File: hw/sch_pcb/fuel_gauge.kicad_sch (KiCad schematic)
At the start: 39 parts

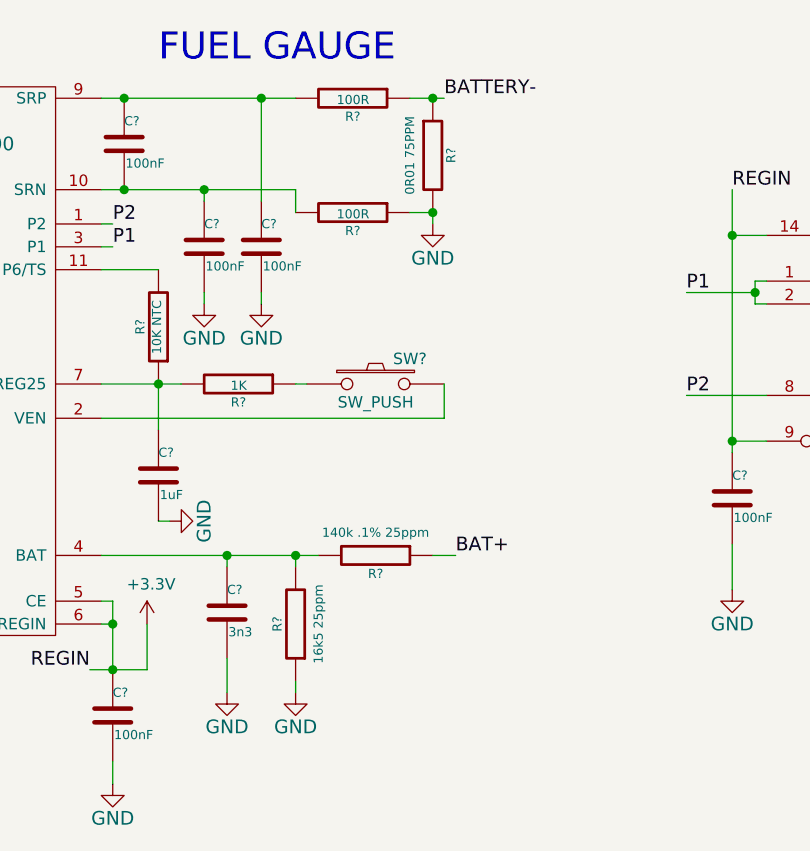
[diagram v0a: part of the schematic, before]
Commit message: Adding input switching regulator.
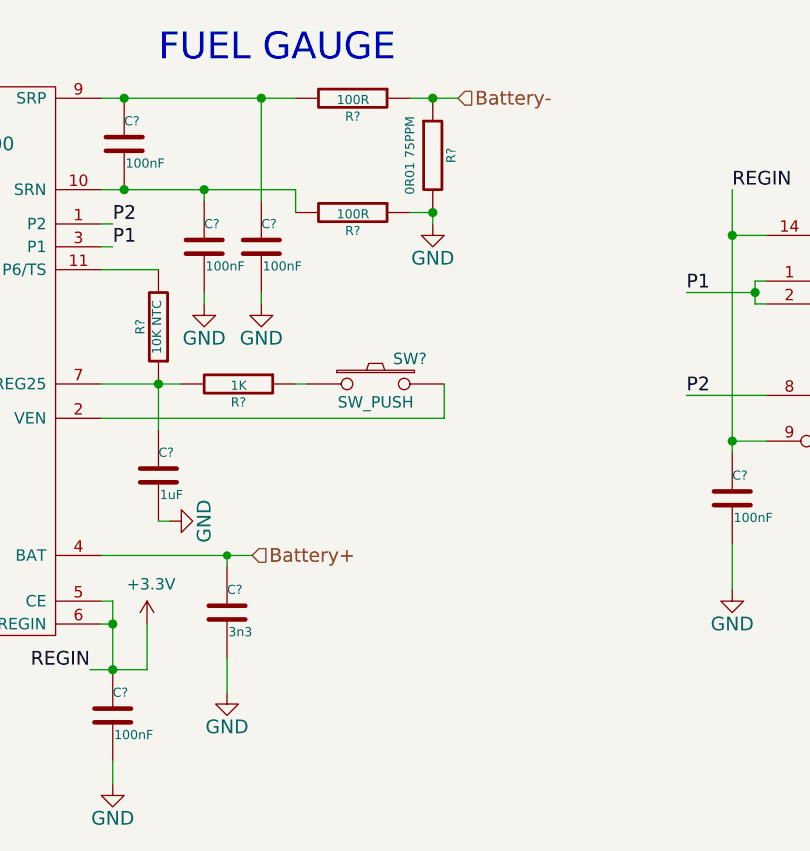
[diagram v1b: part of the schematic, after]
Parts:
- removed R?: 16k5 25ppm, Mlab_R:SMD-0805, symbol LION2CELL01D-rescue:R-RESCUE-LION2CELL01C
- removed R?: 140k .1% 25ppm, Mlab_R:SMD-0805, symbol LION2CELL01D-rescue:R-RESCUE-LION2CELL01C
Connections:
- net Battery+: now reaches C?.1, U?.4 (BAT)
- net BATTERY- renamed Battery-

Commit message: cleanup unused file.
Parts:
- removed J? (x4): JUMP_2x1, Mlab_Pin_Headers:Straight_1x02, symbol LION2CELL01D-rescue:JUMP_2x1
- added P?: HEADER_2x05_PARALLEL, Mlab_Pin_Headers:Straight_2x05, symbol MLAB_HEADER:HEADER_2x05_PARALLEL
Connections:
- net +3V3: no longer C?.1, R?.2, R?.2, U?.5 (CE), U?.6 (REGIN)
- net GND: now also P?.1, P?.10, P?.2, P?.9
- net SCL renamed I2C_SCL
- net I2C_SCL: now also P?.3, P?.4
- net SDA renamed I2C_SDA
- net I2C_SDA: now also P?.7, P?.8
- new net: C?.1, U?.5 (CE)
- new net: P?.5, P?.6
- new net REGIN: R?.2, R?.2
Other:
- moved on the sheet: C?

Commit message: finish gauge schematics design.
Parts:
- added R?: 1k, Mlab_R:SMD-0805, symbol LION2CELL01D-rescue:R-RESCUE-LION2CELL01C
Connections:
- net REGIN is gone; now on net +3V3: R?.2, R?.2
- net +3V3: now also C?.1, P?.5, P?.6, U?.5 (CE), U?.6 (REGIN), R?.2
- net HDQ renamed CHARGE_CTRL
- net CHARGE_CTRL: now also R?.1
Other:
- moved on the sheet: C?, R?

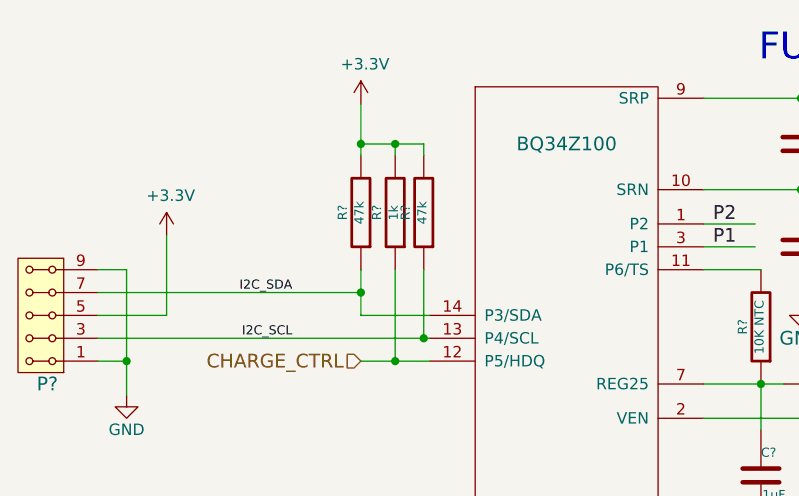
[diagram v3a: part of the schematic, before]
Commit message: Update schematics: Adding datasheet Update title blocks Update pull-up value for CHARGE_CTRL signal.
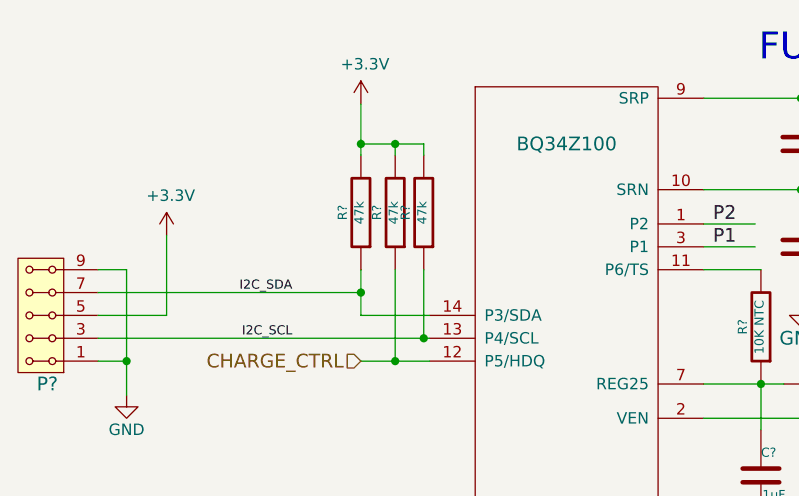
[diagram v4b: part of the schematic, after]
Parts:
- R?: value 1k -> 47k
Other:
- company: (none) -> MLAB.cz
- title: (none) -> SOLARMINIBAT01A
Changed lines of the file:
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@@
   (paper "A4")
   (title_block
+    (title "SOLARMINIBAT01A")
     (date "2022-07-20")
+    (rev "A")
+    (company "MLAB.cz")
     (comment 2 "Solar charged LTO Battery Managment System")
   )
@@
       (effects (font (size 1.524 1.524)) hide)
     )
-    (property "Datasheet" "" (id 3) (at 116.84 84.455 0)
-      (effects (font (size 1.524 1.524)))
+    (property "Datasheet" "https://www.ti.com/lit/ds/symlink/bq34z100-g1.pdf" (id 3) (at 116.84 84.455 0)
+      (effects (font (size 1.524 1.524)) hide)
     )
     (pin "1")
@@
       (effects (font (size 1.016 1.016)))
     )
-    (property "Value" "1k" (id 1) (at 93.8022 80.6704 90)
-      (effects (font (size 1.016 1.016)))
-    )
+    (property "Value" "47k" (id 1) (at 93.8022 80.6704 90)
+      (effects (font (size 1.016 1.016)))
+    )

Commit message: Edit schema
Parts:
- removed R? (x7): 2K2, Mlab_R:SMD-0805, symbol LION2CELL01D-rescue:R-RESCUE-LION2CELL01C
- added R10, R11, R12, R13, R14, R15, R16: 270R, Resistor_SMD:R_0805_2012Metric, symbol LION2CELL01D-rescue:R-RESCUE-LION2CELL01C
- C1, C2, C3, C4, C5, C6, C7: renamed from C?; footprint Mlab_R:SMD-0805 -> Capacitor_SMD:C_0805_2012Metric
- R1, R2, R3, R4, R5, R6, R7: renamed from R?; footprint Mlab_R:SMD-0805 -> Resistor_SMD:R_0805_2012Metric
- R8: renamed from R?; footprint Mlab_R:SMD-2512 -> Resistor_SMD:R_2512_6332Metric_Pad1.40x3.35mm_HandSolder
- R9: renamed from R?; value 2K2 -> 270R; footprint Mlab_R:SMD-0805 -> Resistor_SMD:R_0805_2012Metric
- U2: renamed from U?; footprint Mlab_IO:SO-14 -> Package_SO:SO-14_3.9x8.65mm_P1.27mm
- gave numbers to parts that had none: 11
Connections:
- net at D6.2 (K): now also R14.1
- net at U2.11 (QF): now also R14.2
- net at D2.2 (K): now also R10.1
- net at D3.2 (K): now also R11.1
- net at U2.5 (QC): now also R11.2
- net at D4.2 (K): now also R12.1
- net at D7.2 (K): now also R15.1
- net at U2.6 (QD): now also R12.2
- net at D8.2 (K): now also R16.1
- net at U2.13 (QH): now also R16.2
- net at U2.10 (QE): now also R13.2
- net at U2.12 (QG): now also R15.2
- net at U2.4 (QB): now also R10.2
- net at D5.2 (K): now also R13.1
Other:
- moved on the sheet: C1, C2, C3, C4, C5, C6, C7, D1, D2, D3, D4, D5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

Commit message: Edit PCB
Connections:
- net H: now reaches R16.2, U2.13 (QH)
- net G: now reaches R15.2, U2.12 (QG)
- net C: now reaches R11.2, U2.5 (QC)
- net E: now reaches R13.2, U2.10 (QE)
- net F: now reaches R14.2, U2.11 (QF)
- net A: now reaches R9.2, U2.3 (QA)
- net B: now reaches R10.2, U2.4 (QB)
- net D: now reaches R12.2, U2.6 (QD)
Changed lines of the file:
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@@
     (effects (font (size 2.9972 2.9972)) (justify left bottom))
+  )
+  (label "G" (at 219.71 106.68 0)
+    (effects (font (size 1.524 1.524)) (justify left bottom))
+  )
+  (label "H" (at 219.71 110.49 0)
+    (effects (font (size 1.524 1.524)) (justify left bottom))
   )
   (label "I2C_SCL" (at 69.215 95.25 180)
@@
     (effects (font (size 1.524 1.524)) (justify left bottom))
   )
+  (label "A" (at 219.71 83.82 0)
+    (effects (font (size 1.524 1.524)) (justify left bottom))
+  )
+  (label "C" (at 219.71 91.44 0)
+    (effects (font (size 1.524 1.524)) (justify left bottom))
+  )
+  (label "F" (at 219.7724 102.87 0)
+    (effects (font (size 1.524 1.524)) (justify left bottom))
+  )
+  (label "D" (at 219.71 95.25 0)
+    (effects (font (size 1.524 1.524)) (justify left bottom))
+  )
   (label "P2" (at 179.705 101.6 0)
+    (effects (font (size 1.524 1.524)) (justify left bottom))
+  )
+  (label "E" (at 219.71 99.06 0)
     (effects (font (size 1.524 1.524)) (justify left bottom))
   )
@@
     (effects (font (size 1.016 1.016)) (justify right bottom))
   )
+  (label "B" (at 219.71 87.63 0)
+    (effects (font (size 1.524 1.524)) (justify left bottom))
+  )
   (label "P1" (at 179.705 90.17 0)

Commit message: Edit PCB
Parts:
- R4: footprint Resistor_SMD:R_0805_2012Metric -> Resistor_SMD:R_0805_2012Metric_Pad1.20x1.40mm_HandSolder
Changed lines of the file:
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@@
       (effects (font (size 1.016 1.016)))
     )
-    (property "Footprint" "Resistor_SMD:R_0805_2012Metric" (id 2) (at 123.063 93.98 90)
+    (property "Footprint" "Resistor_SMD:R_0805_2012Metric_Pad1.20x1.40mm_HandSolder" (id 2) (at 123.063 93.98 90)
       (effects (font (size 0.762 0.762)) hide)
     )

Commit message: Edit PCB
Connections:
- net NTC1: now reaches R4.2, U1.11 (P6/TS)
- net NTC2: now reaches C2.1, R4.1, R5.2, U1.7 (REG25)
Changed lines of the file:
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@@
     (comment 2 "Solar charged LTO Battery Managment System")
   )
+  (junction (at 118.11 87.63) (diameter 0) (color 0 0 0 0)
+  )
   (junction (at 121.285 100.33) (diameter 0) (color 0 0 0 0)
   )
@@
   (junction (at 50.8 97.79) (diameter 0) (color 0 0 0 0)
   )
+  (junction (at 118.11 100.33) (diameter 0) (color 0 0 0 0)
+  )
   (junction (at 248.285 106.68) (diameter 1.016) (color 0 0 0 0)
   )
@@
     (stroke (width 0) (type solid) (color 0 0 0 0))
   )
+  (wire (pts (xy 118.11 87.63) (xy 121.285 87.63))
+    (stroke (width 0) (type default) (color 0 0 0 0))
+  )
   (wire (pts (xy 219.075 110.49) (xy 221.615 110.49))
     (stroke (width 0) (type solid) (color 0 0 0 0))
@@
     (stroke (width 0) (type solid) (color 0 0 0 0))
   )
+  (wire (pts (xy 118.11 100.33) (xy 121.285 100.33))
+    (stroke (width 0) (type default) (color 0 0 0 0))
+  )
   (wire (pts (xy 248.285 91.44) (xy 248.285 95.25))
     (stroke (width 0) (type solid) (color 0 0 0 0))
@@
     (stroke (width 0) (type default) (color 0 0 0 0))
   )
+  (wire (pts (xy 118.11 87.63) (xy 118.11 89.535))
+    (stroke (width 0) (type default) (color 0 0 0 0))
+  )
   (wire (pts (xy 83.82 74.93) (xy 83.82 73.66))
     (stroke (width 0) (type default) (color 0 0 0 0))
@@
     (stroke (width 0) (type default) (color 0 0 0 0))
   )
+  (wire (pts (xy 118.11 95.885) (xy 118.11 100.33))
+    (stroke (width 0) (type default) (color 0 0 0 0))
+  )
   (wire (pts (xy 187.325 88.9) (xy 188.595 88.9))
     (stroke (width 0) (type solid) (color 0 0 0 0))
@@
     (stroke (width 0) (type solid) (color 0 0 0 0))
   )
-  (wire (pts (xy 114.935 87.63) (xy 121.285 87.63))
+  (wire (pts (xy 114.935 87.63) (xy 118.11 87.63))
     (stroke (width 0) (type default) (color 0 0 0 0))
   )
@@
     (stroke (width 0) (type solid) (color 0 0 0 0))
   )
-  (wire (pts (xy 114.935 100.33) (xy 121.285 100.33))
+  (wire (pts (xy 114.935 100.33) (xy 118.11 100.33))
     (stroke (width 0) (type default) (color 0 0 0 0))
   )
@@
     (effects (font (size 1.524 1.524)) (justify left))
   )
+  (hierarchical_label "NTC1" (shape input) (at 118.11 89.535 180)
+    (effects (font (size 1.524 1.524)) (justify right))
+  )
+  (hierarchical_label "NTC2" (shape input) (at 118.11 95.885 180)
+    (effects (font (size 1.524 1.524)) (justify right))
+  )
   (symbol (lib_id "LION2CELL01D-rescue:R-RESCUE-LION2CELL01C") (at 227.965 110.49 270) (unit 1)
